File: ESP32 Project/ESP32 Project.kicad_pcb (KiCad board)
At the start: 2 copper layers, 15 x 17.5 mm, 1 part, among them J1 USB_C_Receptacle

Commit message: something more done
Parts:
- added U1: MCP73871, Package_DFN_QFN:QFN-20-1EP_4x4mm_P0.5mm_EP2.5x2.5mm, F.Cu at (122.7, 76.0)
- J1: value USB_C_Receptacle -> 2338792-1; footprint Connector_USB:USB_C_Receptacle_Amphenol_12401548E4-2A -> 2338792-1:TE_2338792-1
- moved J1 3.28 mm to (125.6, 71.2)
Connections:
- J1 pad A1: Net-(J1-GND-PadA1) -> GND_A
- J1 pad A12: Net-(J1-GND-PadA1) -> GND_A
- J1 pad A4: Net-(J1-VBUS-PadA4) -> VBUS_A
- J1 pad A9: Net-(J1-VBUS-PadA4) -> VBUS_A
- J1 pad B1: Net-(J1-GND-PadA1) -> GND_B
- J1 pad B12: Net-(J1-GND-PadA1) -> GND_B
- J1 pad B4: Net-(J1-VBUS-PadA4) -> VBUS_B
- J1 pad B9: Net-(J1-VBUS-PadA4) -> VBUS_B

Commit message: schema is done
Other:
- copper layers 2 -> 4
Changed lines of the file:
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@@
 	(layers
 		(0 "F.Cu" signal)
+		(4 "In1.Cu" power)
+		(6 "In2.Cu" power)
 		(2 "B.Cu" signal)
 		(9 "F.Adhes" user "F.Adhesive")
@@
 			)
 			(layer "dielectric 1"
+				(type "prepreg")
+				(thickness 0.1)
+				(material "FR4")
+				(epsilon_r 4.5)
+				(loss_tangent 0.02)
+			)
+			(layer "In1.Cu"
+				(type "copper")
+				(thickness 0.035)
+			)
+			(layer "dielectric 2"
 				(type "core")
-				(thickness 1.51)
+				(thickness 1.24)
+				(material "FR4")
+				(epsilon_r 4.5)
+				(loss_tangent 0.02)
+			)
+			(layer "In2.Cu"
+				(type "copper")
+				(thickness 0.035)
+			)
+			(layer "dielectric 3"
+				(type "prepreg")
+				(thickness 0.1)
 				(material "FR4")
 				(epsilon_r 4.5)
@@
 		(capping no)
 		(filling no)
+		(zone_defaults)
 		(pcbplotparams
 			(layerselection 0x00000000_00000000_55555555_5755f5ff)

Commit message: something done lmao
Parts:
- added C1: 0.1u, Capacitor_SMD:C_0805_2012Metric, F.Cu at (98.2, 45.8)
- added C10: 0.1, Capacitor_SMD:C_0805_2012Metric, F.Cu at (71.2, 59.9)
- added C11: 1u, Capacitor_SMD:C_0805_2012Metric, F.Cu at (71.2, 62.9)
- added C12: 10u, Capacitor_SMD:C_Elec_5x5.4, F.Cu at (62.1, 70.0)
- added C13: 0.1u, Capacitor_SMD:C_0805_2012Metric, F.Cu at (71.2, 65.9)
- added C14: 0.1u, Capacitor_SMD:C_0805_2012Metric, F.Cu at (71.2, 68.9)
- added C15: 0.1u, Capacitor_SMD:C_0805_2012Metric, F.Cu at (81.7, 59.9)
- added C18: 0.1uf, Capacitor_SMD:C_0805_2012Metric, F.Cu at (81.7, 62.9)
- added C19: 1u, Capacitor_SMD:C_0805_2012Metric, F.Cu at (81.7, 65.9)
- added C2: 0.1u, Capacitor_SMD:C_0805_2012Metric, F.Cu at (98.2, 48.9)
- added C20: 100pf, Capacitor_SMD:C_0805_2012Metric, F.Cu at (81.7, 68.9)
- added C21: 0.1u, Capacitor_SMD:C_0805_2012Metric, F.Cu at (43.6, 92.6)
- added C22: 0.1u, Capacitor_SMD:C_0805_2012Metric, F.Cu at (43.6, 95.7)
- added C24: 0.01uf, Capacitor_SMD:C_0805_2012Metric, F.Cu at (81.7, 71.9)
- added C25: 0.1uf, Capacitor_SMD:C_0805_2012Metric, F.Cu at (81.7, 74.9)
- added C3: 10u, Capacitor_SMD:C_Elec_5x5.4, F.Cu at (92.2, 39.2)
- added C4: 10u, Capacitor_SMD:C_Elec_5x5.4, F.Cu at (92.2, 45.1)
- added C5: 0.1u, Capacitor_SMD:C_0805_2012Metric, F.Cu at (98.2, 51.9)
- added C6: 1u, Capacitor_SMD:C_0805_2012Metric, F.Cu at (98.2, 54.9)
- added C7: 10u, Capacitor_SMD:C_Elec_5x5.4, F.Cu at (62.1, 58.3)
- added C8: 0.1, Capacitor_SMD:C_0805_2012Metric, F.Cu at (71.2, 56.9)
- added C9: 4.7u, Capacitor_SMD:C_Elec_5x5.4, F.Cu at (62.1, 64.2)
- added D1: LED_blue, LED_SMD:LED_0805_2012Metric_Pad1.15x1.40mm_HandSolder, F.Cu at (81.9, 42.9)
- added D2: LED_green, LED_SMD:LED_0805_2012Metric_Pad1.15x1.40mm_HandSolder, F.Cu at (81.9, 46.0)
- added D3: LEDred, LED_SMD:LED_0805_2012Metric_Pad1.15x1.40mm_HandSolder, F.Cu at (81.9, 49.0)
- added D4: LED_red, LED_SMD:LED_0805_2012Metric_Pad1.15x1.40mm_HandSolder, F.Cu at (81.9, 52.0)
- added D5: LED_blue, LED_SMD:LED_0805_2012Metric_Pad1.15x1.40mm_HandSolder, F.Cu at (69.5, 49.9)
- added D6: LED_green, LED_SMD:LED_0805_2012Metric_Pad1.15x1.40mm_HandSolder, F.Cu at (69.5, 52.9)
- added F1: 0ZCH0110AF2E, 0ZCH0110AF2E:FUSC3225X100N, F.Cu at (91.1, 50.2)
- added J2: B2B-PH-SM4-TB, B2B-PH-SM4-TB:JST_B2B-PH-SM4-TB, F.Cu at (93.2, 29.9)
- added J3: GSD090012SEU, GSD090012SEU:AMPHENOL_GSD090012SEU, F.Cu at (170.2, 128.6)
- added J4: Conn_01x04_Pin, Connector_PinHeader_2.54mm:PinHeader_1x04_P2.54mm_Vertical, F.Cu at (43.6, 81.2)
- added J5: Conn_01x05_Pin, Connector_PinHeader_2.54mm:PinHeader_1x05_P2.54mm_Vertical, F.Cu at (39.0, 81.2)
- added MK1: CMC-5042PF-AC, CMC-5042PF-AC:CUI_CMC-5042PF-AC, F.Cu at (87.7, 71.0)
- added Q1: TEMT6000X01, TEMT6000X01:TRANS_TEMT6000X01, F.Cu at (87.6, 76.6)
- added Q2: BC817, Package_TO_SOT_SMD:SOT-23, F.Cu at (48.4, 81.2)
- added Q3: BC817, Package_TO_SOT_SMD:SOT-23, F.Cu at (48.4, 85.6)
- added R1: 10k, Resistor_SMD:R_0805_2012Metric, F.Cu at (81.7, 28.1)
- added R10: 470, Resistor_SMD:R_0805_2012Metric, F.Cu at (86.1, 39.9)
- added R11: 1k, Resistor_SMD:R_0805_2012Metric, F.Cu at (69.3, 28.1)
- added R12: 22k1, Resistor_SMD:R_0805_2012Metric, F.Cu at (69.3, 31.1)
- added R13: 47k5, Resistor_SMD:R_0805_2012Metric, F.Cu at (69.3, 34.0)
- added R14: 470, Resistor_SMD:R_0805_2012Metric, F.Cu at (69.3, 37.0)
- added R15: 50, Resistor_SMD:R_0805_2012Metric, F.Cu at (69.3, 39.9)
- added R16: 50, Resistor_SMD:R_0805_2012Metric, F.Cu at (73.7, 28.1)
- added R18: 470, Resistor_SMD:R_0805_2012Metric, F.Cu at (73.7, 31.1)
- added R19: 10k, Resistor_SMD:R_0805_2012Metric, F.Cu at (73.7, 34.0)
- added R2: 10K, Resistor_SMD:R_0805_2012Metric, F.Cu at (81.7, 31.1)
- added R20: 50, Resistor_SMD:R_0805_2012Metric, F.Cu at (73.7, 37.0)
- added R22: 50, Resistor_SMD:R_0805_2012Metric, F.Cu at (73.7, 39.9)
- added R23: 10k, Resistor_SMD:R_0805_2012Metric, F.Cu at (86.1, 59.9)
- added R24: 4k7, Resistor_SMD:R_0805_2012Metric, F.Cu at (86.1, 62.8)
- added R25: 4k7, Resistor_SMD:R_0805_2012Metric, F.Cu at (86.1, 65.8)
- added R27: 10k, Resistor_SMD:R_0805_2012Metric, F.Cu at (90.5, 59.9)
- added R28: 1M, Resistor_SMD:R_0805_2012Metric, F.Cu at (90.5, 62.8)
- added R29: 1M, Resistor_SMD:R_0805_2012Metric, F.Cu at (90.5, 65.8)
- added R3: 5k1, Resistor_SMD:R_0805_2012Metric, F.Cu at (81.7, 34.0)
- added R30: 2k, Resistor_SMD:R_0805_2012Metric, F.Cu at (94.9, 59.9)
- added R31: 100k, Resistor_SMD:R_0805_2012Metric, F.Cu at (94.9, 62.8)
- added R32: 2k, Resistor_SMD:R_0805_2012Metric, F.Cu at (94.9, 65.8)
- added R33: 10k, Resistor_SMD:R_0805_2012Metric, F.Cu at (53.0, 80.4)
- added R34: 10k, Resistor_SMD:R_0805_2012Metric, F.Cu at (53.0, 83.3)
- added R35: 10k, Resistor_SMD:R_0805_2012Metric, F.Cu at (53.0, 86.3)
- added R4: 5k1, Resistor_SMD:R_0805_2012Metric, F.Cu at (81.7, 37.0)
- added R5: 2k, Resistor_SMD:R_0805_2012Metric, F.Cu at (81.7, 39.9)
- added R6: 20k, Resistor_SMD:R_0805_2012Metric, F.Cu at (86.1, 28.1)
- added R7: 470, Resistor_SMD:R_0805_2012Metric, F.Cu at (86.1, 31.1)
- added R8: 470, Resistor_SMD:R_0805_2012Metric, F.Cu at (86.1, 34.0)
- added R9: 470, Resistor_SMD:R_0805_2012Metric, F.Cu at (86.1, 37.0)
- added S1: USLPT2819DT2TR (BOOT), USLPT2819DT2TR:SW_USLPT2819DT2TR, F.Cu at (48.8, 89.5)
- added S2: USLPT2819DT2TR (RESET), USLPT2819DT2TR:SW_USLPT2819DT2TR, F.Cu at (48.8, 93.0)
- added TP1: TestPoint MOSI, TestPoint:TestPoint_Pad_D1.0mm, F.Cu at (67.5, 56.9)
- added TP2: TestPoint MISO, TestPoint:TestPoint_Pad_D1.0mm, F.Cu at (67.5, 60.0)
- added TP3: TestPoint SCLK, TestPoint:TestPoint_Pad_D1.0mm, F.Cu at (67.5, 63.0)
- added TP4: TestPoint CS-SD, TestPoint:TestPoint_Pad_D1.0mm, F.Cu at (67.5, 66.0)
- added TP5: TestPoint CS, TestPoint:TestPoint_Pad_D1.0mm, F.Cu at (67.5, 69.1)
- added U2: W25Q32JVSSIQ, W25Q32JVSSIQ:SOIC127P790X216-8N, F.Cu at (72.3, 44.9)
- added U3: ESP32-C3-WROOM-02-H4, Esp32 c3 wroom 02:MODULE_ESP32-C3-WROOM-02-H4, F.Cu at (169.2, 80.2)
- added U4: CP2102N-Axx-xQFN20, Package_DFN_QFN:QFN-20-1EP_3x3mm_P0.45mm_EP1.6x1.6mm, F.Cu at (72.1, 73.1)
- added U5: USBLC6-2SC6, Package_TO_SOT_SMD:SOT-23-6, F.Cu at (74.5, 50.8)
- added U6: BME280, Package_LGA:Bosch_LGA-8_2.5x2.5mm_P0.65mm_ClockwisePinNumbering, F.Cu at (93.7, 73.2)
- added U7: MAX4466EXK, MAX4466EXK:SOT65P210X110-5N, F.Cu at (94.2, 69.1)
- added VR1: LM1117MPX-3.3, LM1117MPX-3.3:VREG_LM1117MPX-3.3, F.Cu at (101.3, 40.3)
- moved U1 107.9 mm to (18.4, 48.2)
- moved J1 107.9 mm to (21.4, 43.3)
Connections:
- net Net-(U1-OUT-Pad1) renamed /+5Volt
- J1 pad A1: GND_A -> GND
- J1 pad A12: GND_A -> GND
- J1 pad A5: unconnected-(J1-CC1-PadA5) -> Net-(J1-CC1)
- J1 pad A6: unconnected-(J1-DP1-PadA6) -> /USB-DP
- J1 pad A7: unconnected-(J1-DN1-PadA7) -> /USB-DN
- J1 pad B1: GND_B -> GND
- J1 pad B12: GND_B -> GND
- J1 pad B4: VBUS_B -> VBUS_A
- J1 pad B5: unconnected-(J1-CC2-PadB5) -> Net-(J1-CC2)
- J1 pad B6: unconnected-(J1-DP2-PadB6) -> /USB-DP
- J1 pad B7: unconnected-(J1-DN2-PadB7) -> /USB-DN
- J1 pad B9: VBUS_B -> VBUS_A
- J1 pad G1: Net-(J1-SHIELD-PadG1) -> GND
- J1 pad G2: Net-(J1-SHIELD-PadG1) -> GND
- J1 pad G3: Net-(J1-SHIELD-PadG1) -> GND
- J1 pad G4: Net-(J1-SHIELD-PadG1) -> GND
- J1 pad G5: Net-(J1-SHIELD-PadG1) -> GND
- J1 pad G6: Net-(J1-SHIELD-PadG1) -> GND
- U1 pad 10: Net-(U1-V_{SS}-Pad10) -> GND
- U1 pad 11: Net-(U1-V_{SS}-Pad10) -> GND
- U1 pad 12: unconnected-(U1-PROG3-Pad12) -> Net-(U1-PROG3)
- U1 pad 13: unconnected-(U1-PROG1-Pad13) -> Net-(U1-PROG1)
- U1 pad 14: Net-(U1-V_{BAT}-Pad14) -> /Vbat
- U1 pad 15: Net-(U1-V_{BAT}-Pad14) -> /Vbat
- U1 pad 16: unconnected-(U1-V_{BAT_SENSE}-Pad16) -> /Vbat
- U1 pad 17: unconnected-(U1-CE-Pad17) -> /5volt usb
- U1 pad 18: Net-(U1-IN-Pad18) -> /5volt usb
- U1 pad 19: Net-(U1-IN-Pad18) -> /5volt usb
- U1 pad 2: unconnected-(U1-VPCC-Pad2) -> /5volt usb
- U1 pad 21: Net-(U1-V_{SS}-Pad10) -> GND
- U1 pad 3: unconnected-(U1-SEL-Pad3) -> GND
- U1 pad 4: unconnected-(U1-PROG2-Pad4) -> /5volt usb
- U1 pad 5: unconnected-(U1-THERM-Pad5) -> Net-(U1-THERM)
- U1 pad 6: unconnected-(U1-~{PG}-Pad6) -> /Charging
- U1 pad 7: unconnected-(U1-STAT2-Pad7) -> /Charging power good
- U1 pad 8: unconnected-(U1-STAT1/~{LBO}-Pad8) -> /charged
- U1 pad 9: unconnected-(U1-~{TE}-Pad9) -> Net-(U1-~{TE})
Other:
- board size 15 x 17.5 mm -> 1 x 0.7 mm

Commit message: pcb ont he way tomoroow
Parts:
- C12, C3, C4, C7, C9: footprint Capacitor_SMD:C_Elec_5x5.4 -> Capacitor_Tantalum_SMD:CP_EIA-6032-28_Kemet-C
- moved R16 175.1 mm to (242.4, 75.0)
- moved R19 175.1 mm to (242.4, 80.8)
- moved C7 175.0 mm to (236.1, 39.7)
- moved C8 175.0 mm to (245.3, 38.3)
- moved C12 171.3 mm to (233.1, 81.1)
- moved C13 165.4 mm to (236.3, 77.2)
- moved J1 164.6 mm to (169.4, 115.1)
- moved R15 158.6 mm to (226.3, 62.7)
- moved R20 154.3 mm to (226.6, 57.9)
- moved C21 147.0 mm to (190.2, 102.4)
- moved C22 147.0 mm to (190.2, 105.4)
- moved Q2 147.0 mm to (195.0, 90.9)
- moved Q3 147.0 mm to (195.0, 95.4)
- moved R33 147.0 mm to (199.7, 90.2)
- moved R34 147.0 mm to (199.7, 93.1)
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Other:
- board size 1 x 0.7 mm -> 135 x 85 mm

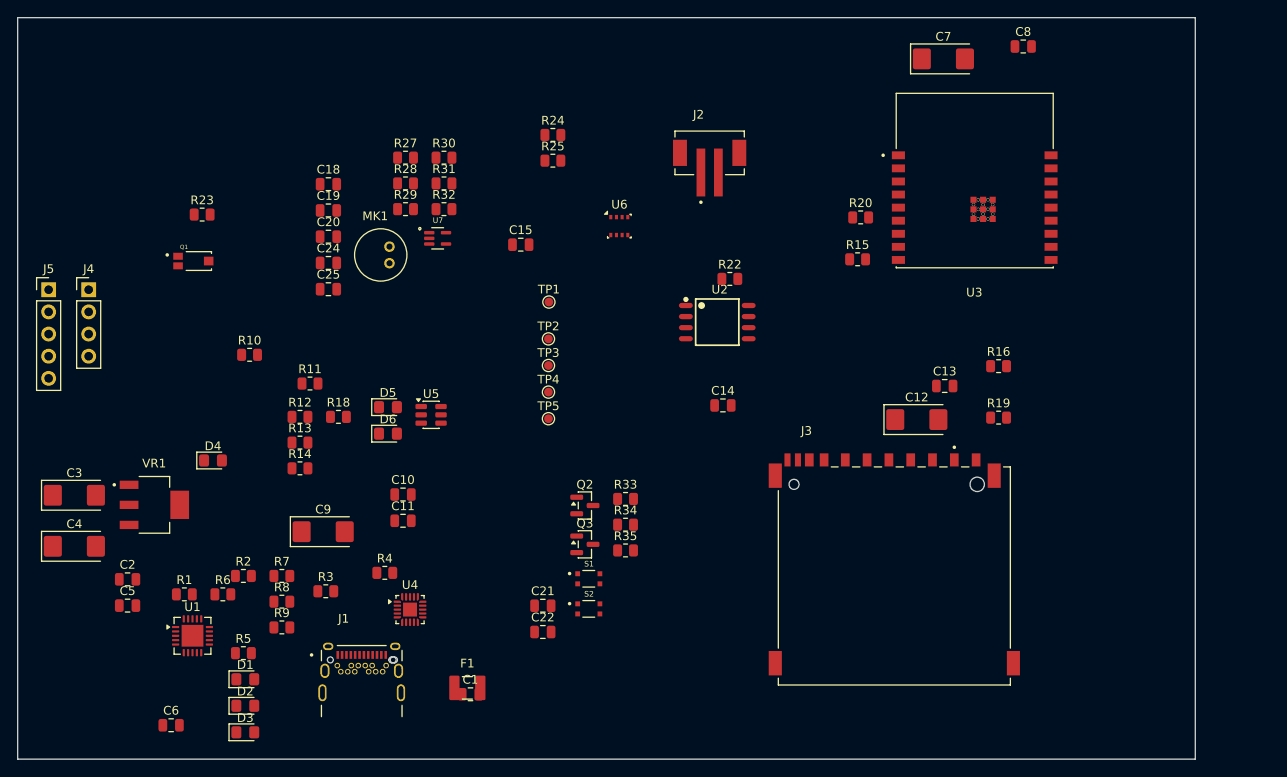
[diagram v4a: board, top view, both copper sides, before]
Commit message: pcb done and some 3d models aadd
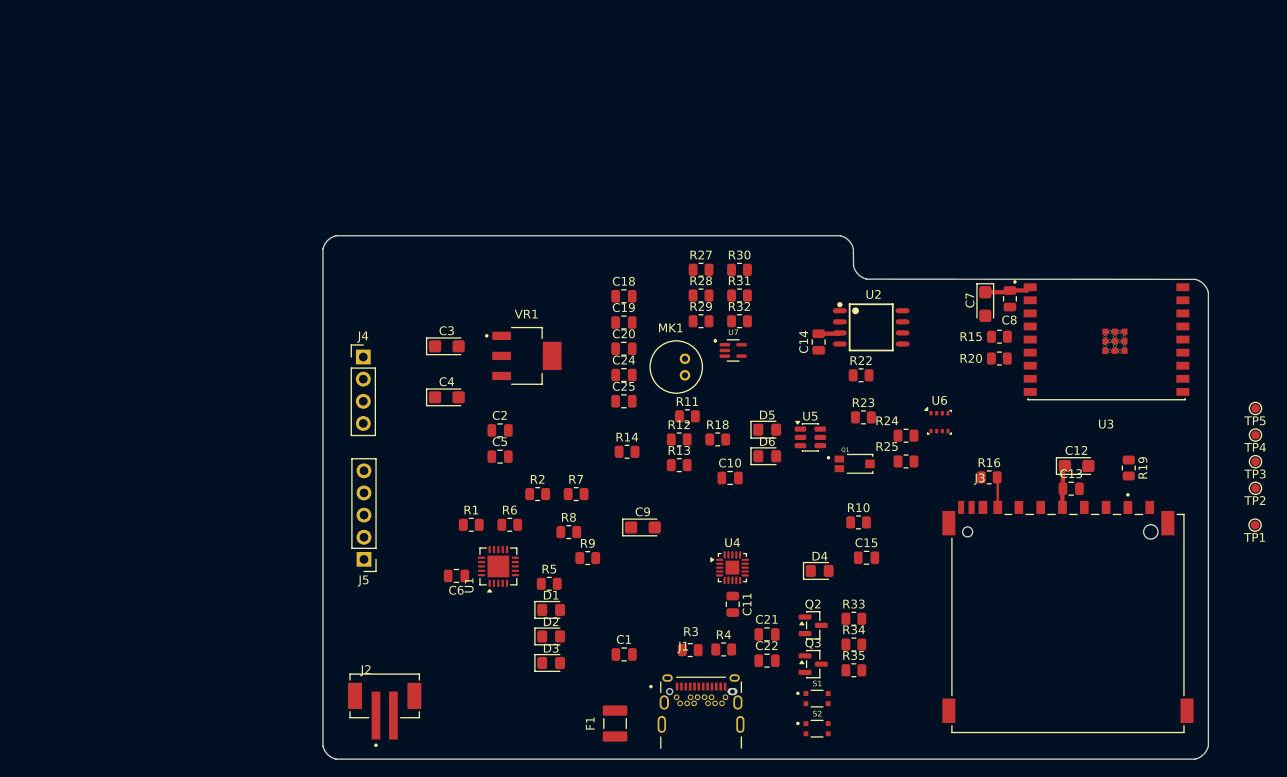
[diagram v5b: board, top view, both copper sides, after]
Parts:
- C12, C3, C4, C7, C9: footprint Capacitor_Tantalum_SMD:CP_EIA-6032-28_Kemet-C -> Capacitor_Tantalum_SMD:CP_EIA-3216-12_Kemet-S
- moved TP1 84.9 mm to (271.9, 93.2), turned to 180 degrees
- moved TP2 82.8 mm to (271.9, 89.0), turned to 180 degrees
- moved TP3 81.8 mm to (271.9, 85.9), turned to 180 degrees
- moved TP4 81.2 mm to (271.9, 82.8), turned to 180 degrees
- moved TP5 81.1 mm to (271.9, 79.8), turned to 180 degrees
- moved R23 79.3 mm to (227.0, 80.8)
- moved Q1 79.3 mm to (225.9, 86.2)
- moved J2 72.5 mm to (172.1, 112.8)
- moved R10 72.4 mm to (226.4, 92.9)
- moved D4 70.7 mm to (221.9, 98.4)
- moved C15 53.5 mm to (227.3, 96.9)
- moved R24 53.2 mm to (231.8, 82.9)
- moved R25 53.2 mm to (231.8, 85.9)
- moved J5 47.6 mm to (169.7, 97.1), turned to 180 degrees
- moved C2 46.0 mm to (185.3, 82.3)
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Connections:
- C11 pad 1: Net-(U4-VBUS) -> VBUS_A
- R12 pad 2: Net-(U4-VBUS) -> VBUS_A
- R13 pad 1: Net-(U4-VBUS) -> VBUS_A
- U4 pad 8: Net-(U4-VBUS) -> VBUS_A
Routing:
- net +3.3V: track 0.00 -> 13.0 mm
- net Net-(J3-DAT0): track 0.00 -> 3.48 mm
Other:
- board size 135 x 85 mm -> 101.5 x 60 mm

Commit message: half pcb done
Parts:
- moved D5 82.4 mm to (151.5, 133.7)
- moved D6 82.4 mm to (151.5, 136.7)
- moved R11 82.3 mm to (147.3, 137.5)
- moved R12 82.3 mm to (146.3, 140.2)
- moved R14 82.3 mm to (140.4, 141.6)
- moved R18 82.3 mm to (150.8, 140.2)
- moved R13 78.9 mm to (150.8, 142.8)
- moved C4 28.6 mm to (207.0, 85.3), turned to 90 degrees
- moved C3 27.8 mm to (196.9, 94.1)
- moved U5 27.3 mm to (208.0, 107.2), turned to -90 degrees
- moved C15 27.1 mm to (216.4, 72.1)
- moved R2 23.1 mm to (182.7, 111.7), turned to -90 degrees
- moved U6 22.9 mm to (216.4, 69.1)
- moved R7 22.5 mm to (186.7, 110.9), turned to 180 degrees
- moved R25 21.1 mm to (219.3, 68.9), turned to 90 degrees
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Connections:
- C19 pad 1: Net-(C19-Pad1) -> Net-(U7-IN-)
- R27 pad 1: Net-(C19-Pad1) -> Net-(U7-IN-)
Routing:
- net /Charging: track 0.00 -> 7.82 mm
- net /Charging power good: track 0.00 -> 5.82 mm
- net /Esp32-C2-02/MIC-OUT: track 0.00 -> 5.63 mm
- net Net-(U7-IN-): track 0.00 -> 5.59 mm
- net /+5Volt: track 0.00 -> 5.18 mm
- net /charged: track 0.00 -> 4.19 mm
- net /Esp32-C2-02/PHOTO-C: track 0.00 -> 3.67 mm
- net +3.3V: track 13.0 -> 16.2 mm
- net Net-(D1-K): track 0.00 -> 2.60 mm
- net Net-(D3-K): track 0.00 -> 2.51 mm
- net Net-(D2-K): track 0.00 -> 2.51 mm
- net Net-(U1-PROG1): track 0.00 -> 2.41 mm
- net Net-(U1-PROG3): track 0.00 -> 2.40 mm
- net /5volt usb: track 0.00 -> 2.12 mm

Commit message: Half and more pcb done
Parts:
- added Hole 1: MountingHole_2.5mm, MountingHole:MountingHole_2.5mm, F.Cu at (182.4, 83.2)
- added Hole 2: MountingHole_2.5mm, MountingHole:MountingHole_2.5mm, F.Cu at (230.0, 83.2)
- moved R12 91.1 mm to (220.9, 87.8)
- moved R13 87.6 mm to (220.9, 90.3)
- moved R14 83.1 mm to (208.9, 94.7)
- moved R11 82.1 mm to (214.0, 89.6), turned to 90 degrees
- moved R18 75.7 mm to (208.9, 91.7)
- moved D6 67.8 mm to (204.7, 94.6), turned to 180 degrees
- moved D5 67.8 mm to (204.6, 91.6), turned to 180 degrees
- moved J5 45.8 mm to (199.7, 62.5), turned to -90 degrees
- moved J4 37.7 mm to (205.6, 62.5), turned to 90 degrees
- moved PLED 30.7 mm to (196.2, 81.6), turned to -90 degrees
- moved C19 27.9 mm to (217.6, 78.8), turned to 0 degrees
- moved R27 26.0 mm to (217.6, 76.4), turned to 0 degrees
- moved R29 24.9 mm to (217.6, 74.0), turned to 0 degrees
- moved R28 24.8 mm to (217.6, 71.5), turned to 0 degrees
- moved C6 20.2 mm to (195.3, 111.6)
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- renumbered D4 to PLED
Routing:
- net +3.3V: track 16.2 -> 5.67 mm
- net /Charging: track 7.82 -> 0.31 mm
- net /Charging power good: track 5.82 -> 0.00 mm
- net /+5Volt: track 5.18 -> 0.00 mm
- net /Esp32-C2-02/PHOTO-C: track 3.67 -> 0.00 mm
- net /charged: track 4.19 -> 0.55 mm
- net Net-(J3-DAT0): track 3.48 -> 0.00 mm
- net Net-(D1-K): track 2.60 -> 0.07 mm
- net Net-(D3-K): track 2.51 -> 0.00 mm
- net Net-(D2-K): track 2.51 -> 0.00 mm
- net Net-(U1-PROG1): track 2.41 -> 0.00 mm
- net Net-(U1-PROG3): track 2.40 -> 0.00 mm
- net /5volt usb: track 2.12 -> 0.00 mm
- added copper zone on In1.Cu, net +3.3V
- added copper zone on In2.Cu, net GND
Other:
- board size 101.5 x 60 mm -> 89.5 x 55 mm

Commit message: done more work on pcblayout
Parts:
- moved PLED 3.92 mm to (199.9, 83.0), turned to 0 degrees
- moved C2 3.14 mm to (186.5, 87.0)
- moved VR1 2.78 mm to (194.8, 88.3)
- moved C3 2.61 mm to (188.9, 87.5)
- moved D6 2.10 mm to (202.7, 95.3)
- moved D5 2.10 mm to (202.7, 92.3)
- moved R14 2.10 mm to (206.9, 95.3)
- moved R18 2.10 mm to (206.9, 92.3)
- moved C4 1.72 mm to (193.1, 83.4)
- moved R3 1.71 mm to (205.9, 110.7)
- moved R4 1.71 mm to (205.9, 107.0)
- moved R10 1.62 mm to (199.7, 80.3), turned to 180 degrees
- moved U5 1.54 mm to (212.7, 100.8)
- moved C10 1.52 mm to (215.7, 93.9)
- moved R13 1.52 mm to (219.4, 89.8)
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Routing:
- net /Vbat: track 0.00 -> 7.59 mm
- net /Esp32-C2-02/USB D+: track 0.00 -> 4.93 mm
- net /Esp32-C2-02/USB D-: track 0.00 -> 4.93 mm
- net GND: track 0.00 -> 4.29 mm, vias 0 -> 12
- net /USB-DN: track 0.00 -> 4.16 mm
- net /USB-DP: track 0.00 -> 4.06 mm
- net /5volt usb: track 0.00 -> 0.47 mm, vias 0 -> 3
- net VBUS_A: vias 0 -> 3
- net +3.3V: vias 0 -> 5
- added copper zone on F.Cu, net +3.3V
- added copper zone on F.Cu, net /+5Volt
- added copper zone on In1.Cu, net /+5Volt
- added copper zone on F.Cu, net /5volt usb
- added copper zone on F.Cu, net /Vbat
- added copper zone on F.Cu, net GND
- added copper zone on F.Cu, net VBUS_A
- added copper zone on In1.Cu, net VBUS_A
